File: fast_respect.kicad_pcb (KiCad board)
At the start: 2 copper layers, 70 x 110 mm, 97 parts, among them J1_1 Conn_02x04_Odd_Even, J5_1 Conn_02x03_Odd_Even, J5_2 Conn_02x03_Odd_Even, J7_1 Conn_01x02, Q2_1 AONM7421, Q3_1 IRLML6344T, Q4_1 IRLML6344T, Q4_2 IRLML6344T, Q4_3 IRLML6344T, Q4_4 IRLML6344T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

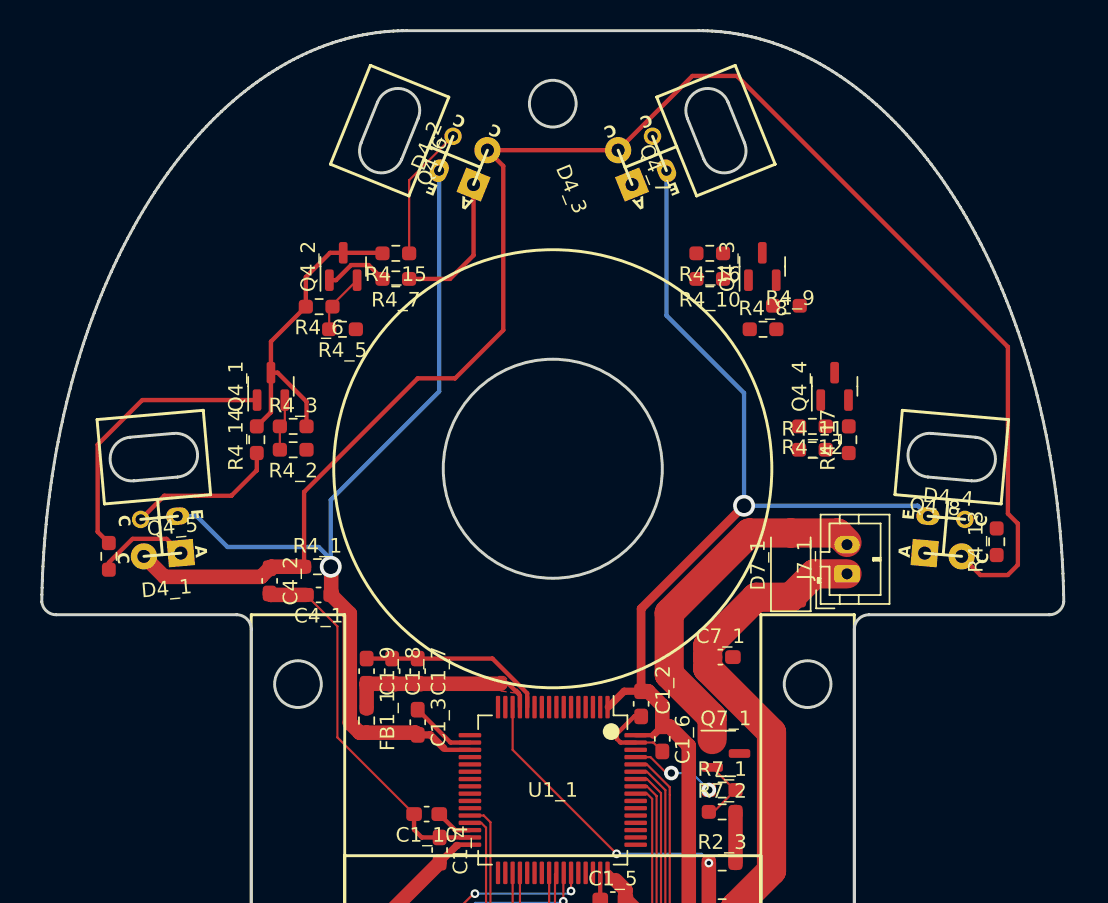
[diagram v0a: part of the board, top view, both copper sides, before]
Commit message: 距離センサ周り引いた
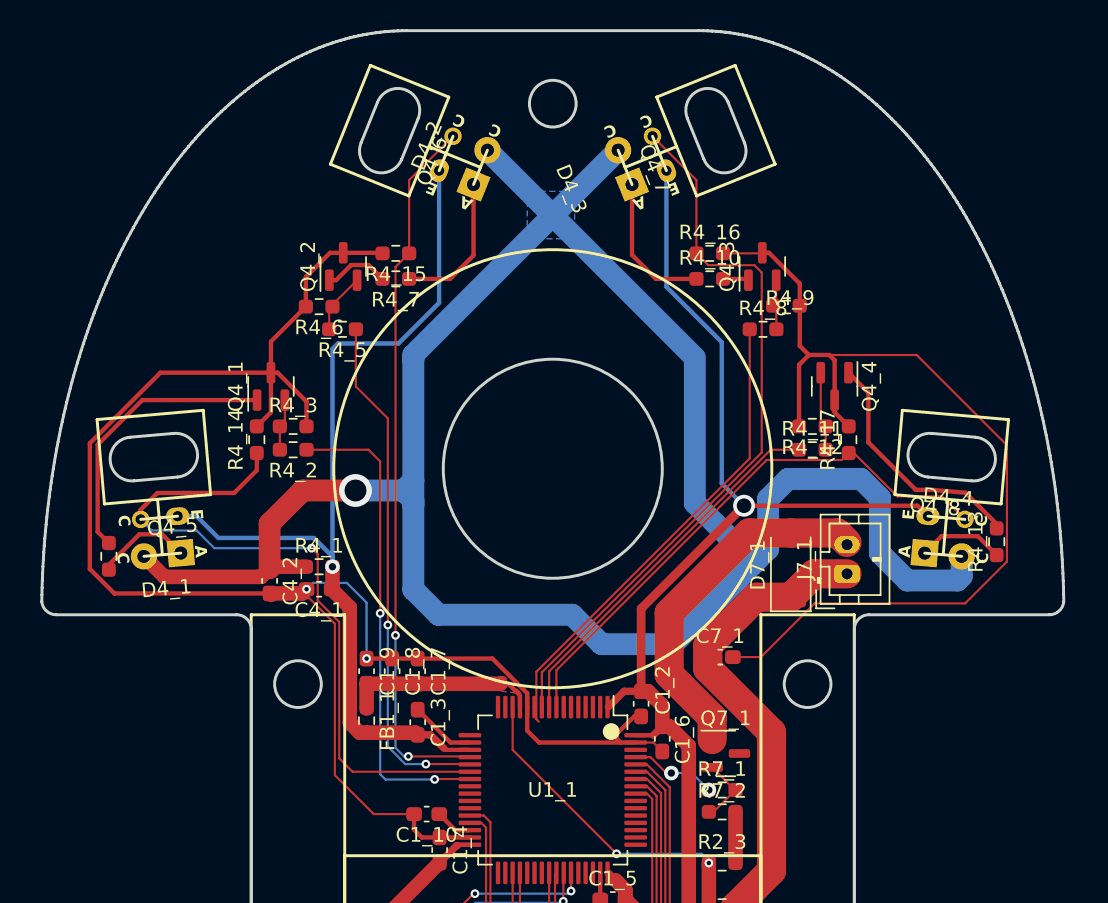
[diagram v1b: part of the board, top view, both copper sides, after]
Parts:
- moved C4_1 0.39 mm to (-51.0, 38.2)
- moved R4_1 0.12 mm to (-51.0, 36.7)
- turned Q4_4 to -90 degrees
- turned R4_10 to 0 degrees
- turned R4_16 to 0 degrees
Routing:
- net GND: track 222.0 -> 346.2 mm, vias 2 -> 4
- net DIST_ADC_3: track 0.00 -> 50.3 mm
- net Net-(D4_1-A): track 113.3 -> 156.0 mm, vias 0 -> 1
- net DIST_ADC_2: track 9.26 -> 48.9 mm, vias 0 -> 2
- net DIST_ADC_4: track 0.00 -> 38.5 mm
- net DIST_ADC_1: track 10.8 -> 48.2 mm, vias 0 -> 1
- net DIST_LED_2: track 0.00 -> 35.6 mm, vias 0 -> 2
- net DIST_LED_1: track 0.14 -> 33.2 mm, vias 0 -> 2
- net DIST_LED_3: track 0.00 -> 33.0 mm
- net DIST_LED_4: track 0.00 -> 25.9 mm
- net Net-(Q4_4-D): track 0.00 -> 16.7 mm
- net Net-(D4_3-K): track 0.00 -> 9.91 mm
- net Net-(D4_4-K): track 0.00 -> 5.95 mm
- net Net-(Q4_4-G): track 0.00 -> 5.42 mm
- net Net-(Q4_3-G): track 0.00 -> 3.86 mm
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- added copper zone on B.Cu, net Net-(D4_1-A)

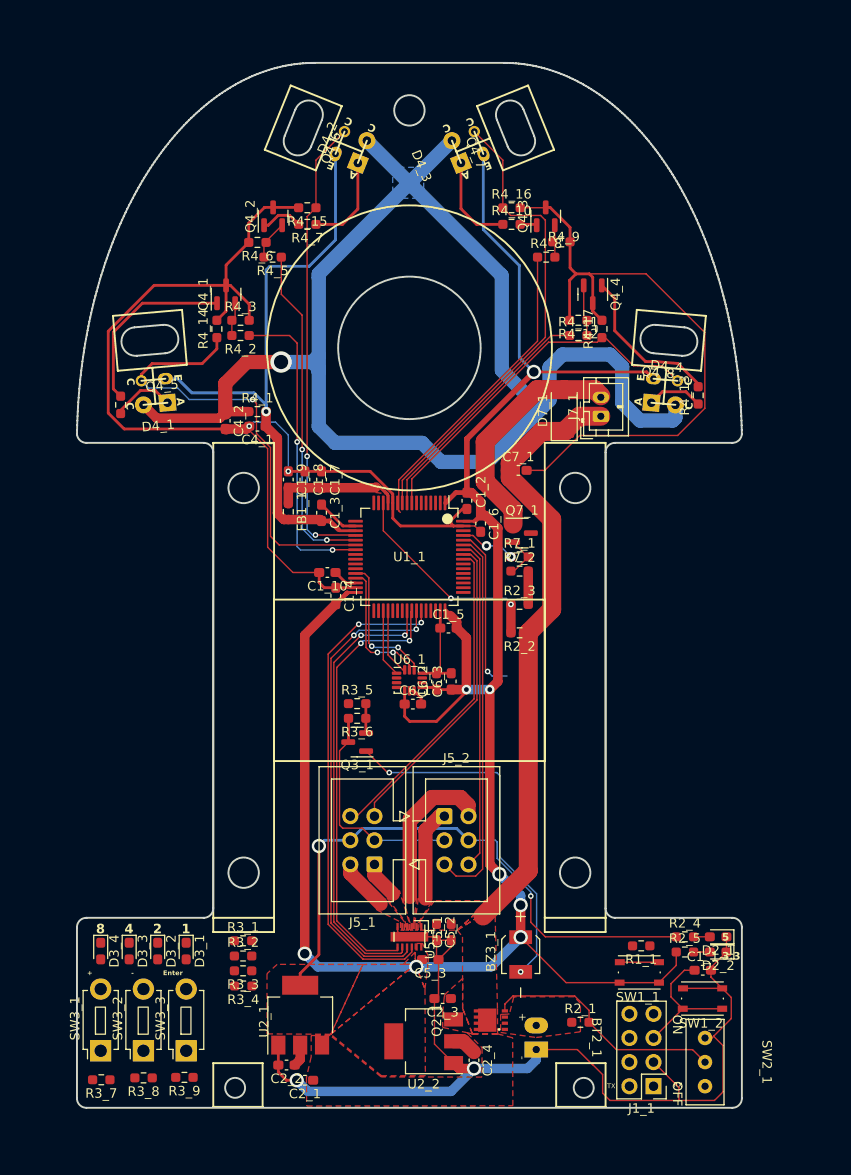
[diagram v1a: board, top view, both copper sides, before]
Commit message: 左側の3.3vのラインを車体前方まで引いた
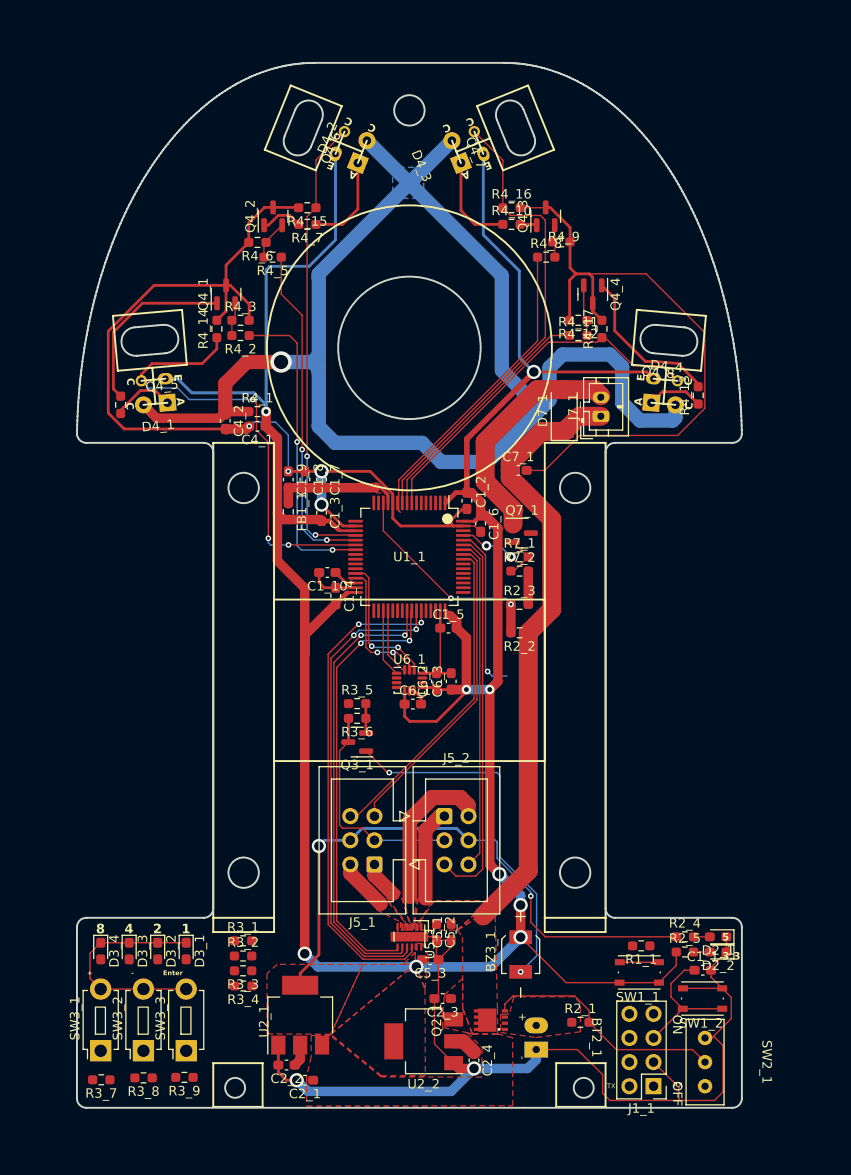
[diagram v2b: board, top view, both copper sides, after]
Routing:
- net +3.3V: track 289.9 -> 305.9 mm
- net GND: track 346.2 -> 353.9 mm, vias 4 -> 6
- net DIST_ADC_1: track 48.2 -> 48.7 mm, vias 1 -> 3

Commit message: 電源周りを整えてUIと書き込み配線以外完成
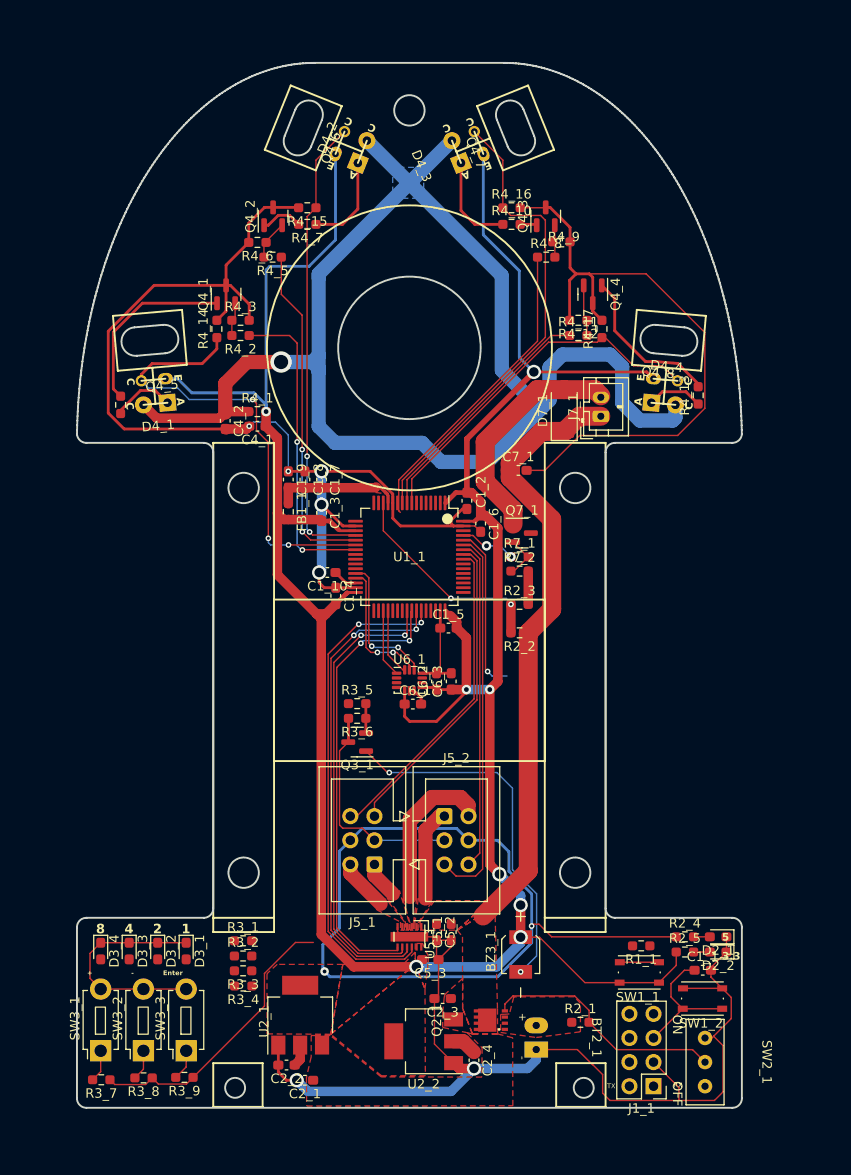
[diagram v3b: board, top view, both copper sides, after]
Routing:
- net +3.3V: track 305.9 -> 330.9 mm, vias 9 -> 8
- net +5V: track 63.8 -> 85.6 mm
- net GND: track 353.9 -> 361.1 mm, vias 6 -> 7
- net UI_SW_1: track 0.00 -> 3.40 mm
- net UI_SW_3: track 0.00 -> 3.26 mm
- net UI_SW_2: track 0.00 -> 3.22 mm

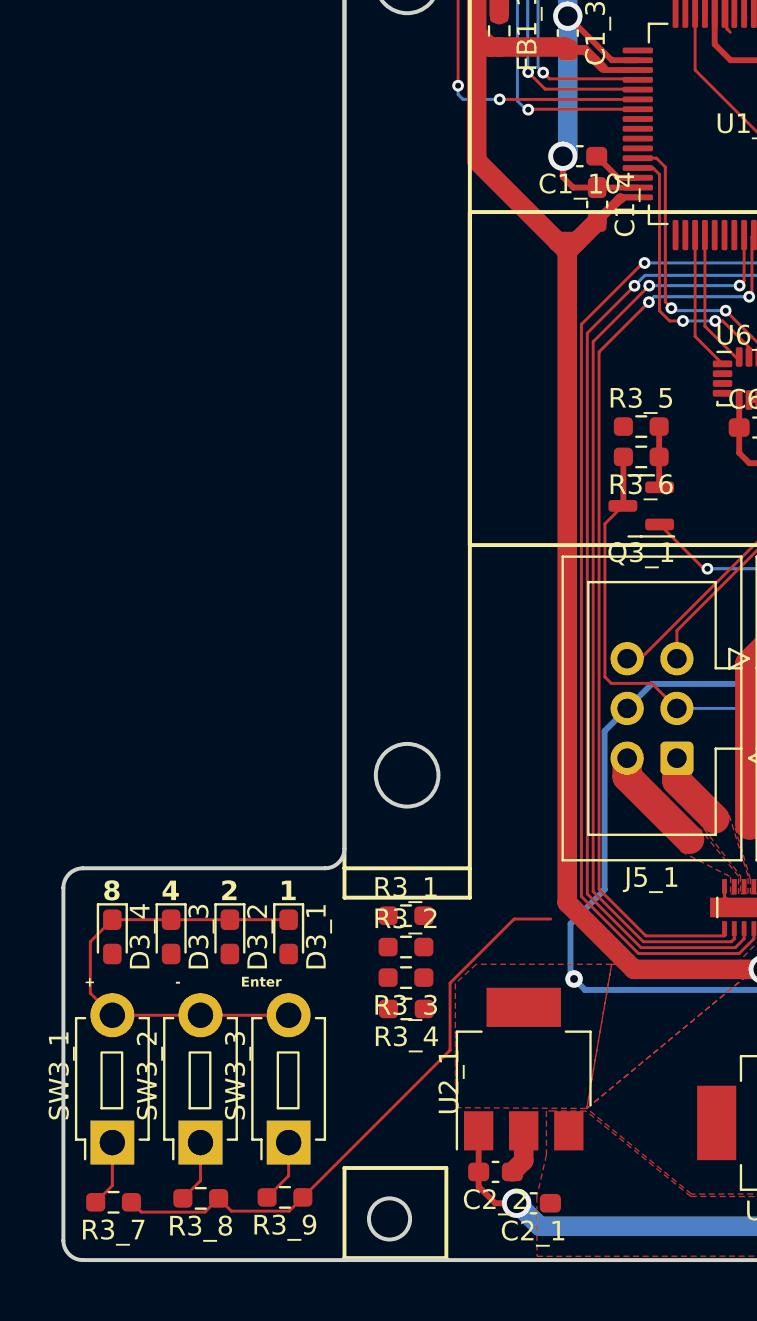
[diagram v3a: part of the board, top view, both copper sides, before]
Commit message: UI_LED接続
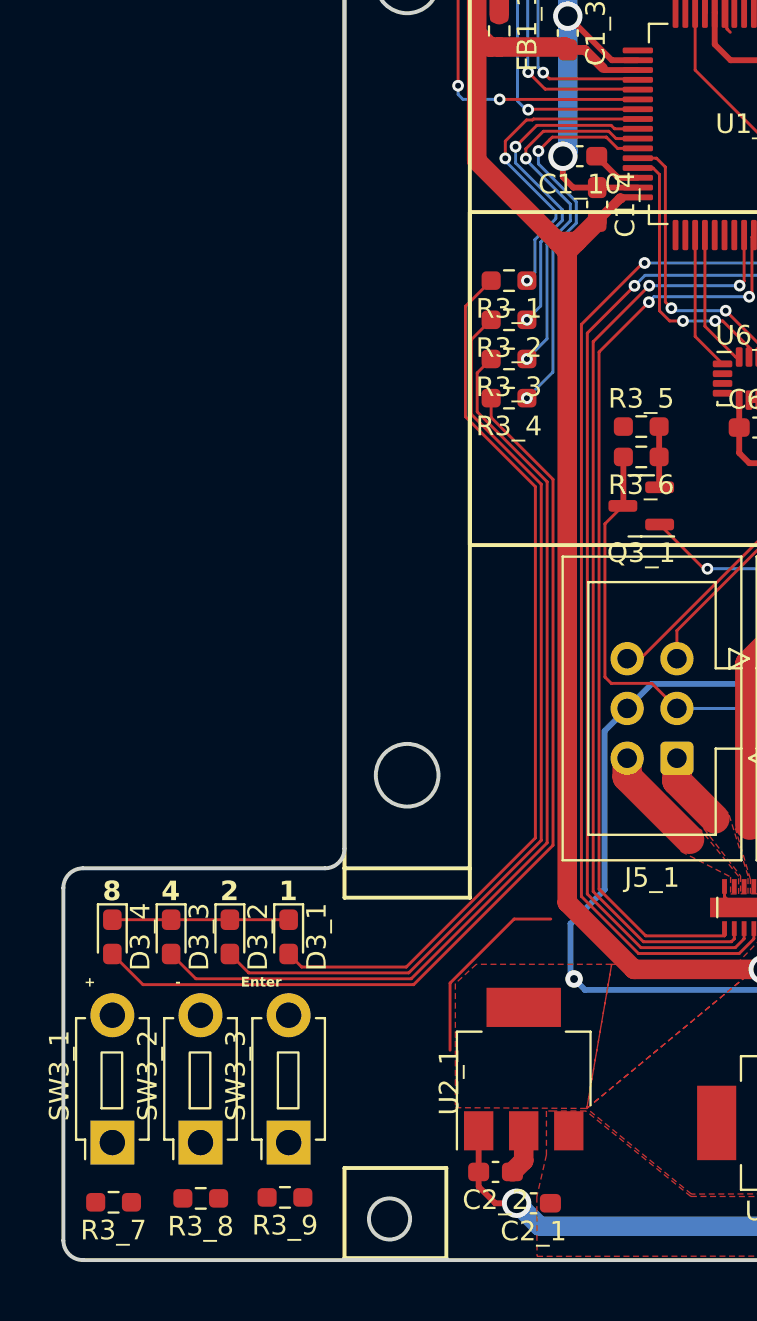
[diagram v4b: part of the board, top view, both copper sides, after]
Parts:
- moved R3_1 32.8 mm to (-47.2, 60.0), turned to 180 degrees
- moved R3_2 32.4 mm to (-47.2, 62.0), turned to 180 degrees
- moved R3_3 32.0 mm to (-47.2, 64.0)
- moved R3_4 31.6 mm to (-47.2, 66.0)
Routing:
- net Net-(D3_4-A): track 0.00 -> 50.2 mm
- net Net-(D3_3-A): track 0.00 -> 49.1 mm
- net Net-(D3_2-A): track 0.00 -> 47.6 mm
- net Net-(D3_1-A): track 0.00 -> 46.1 mm
- net +3.3V: track 330.9 -> 310.5 mm
- net UI_LED_4: track 0.00 -> 20.1 mm, vias 0 -> 2
- net UI_LED_3: track 0.00 -> 18.8 mm, vias 0 -> 2
- net UI_LED_2: track 0.00 -> 17.3 mm, vias 0 -> 2
- net UI_LED_1: track 0.00 -> 16.0 mm, vias 0 -> 2
- net GND: track 361.1 -> 346.3 mm
- net UI_SW_1: track 3.40 -> 0.00 mm
- net UI_SW_3: track 3.26 -> 0.00 mm
- net UI_SW_2: track 3.22 -> 0.00 mm

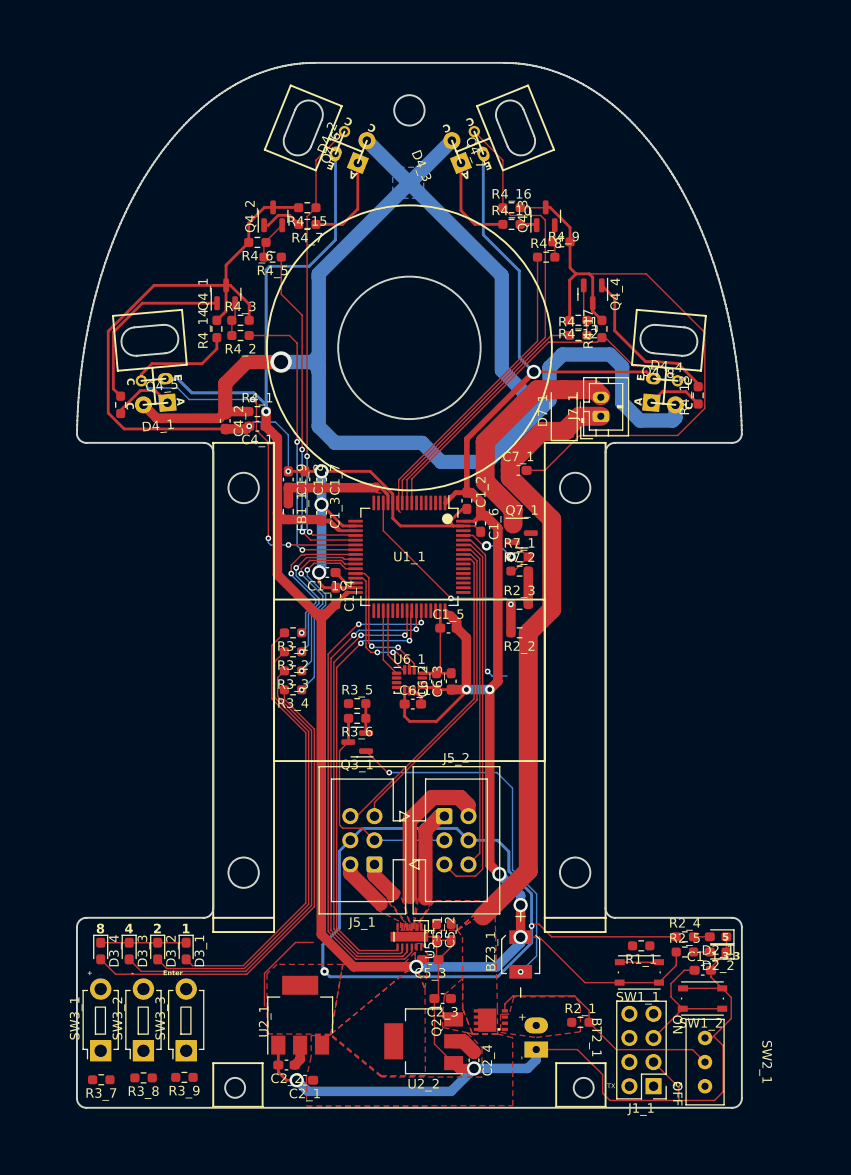
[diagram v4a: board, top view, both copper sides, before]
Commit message: 書き込みピン配線
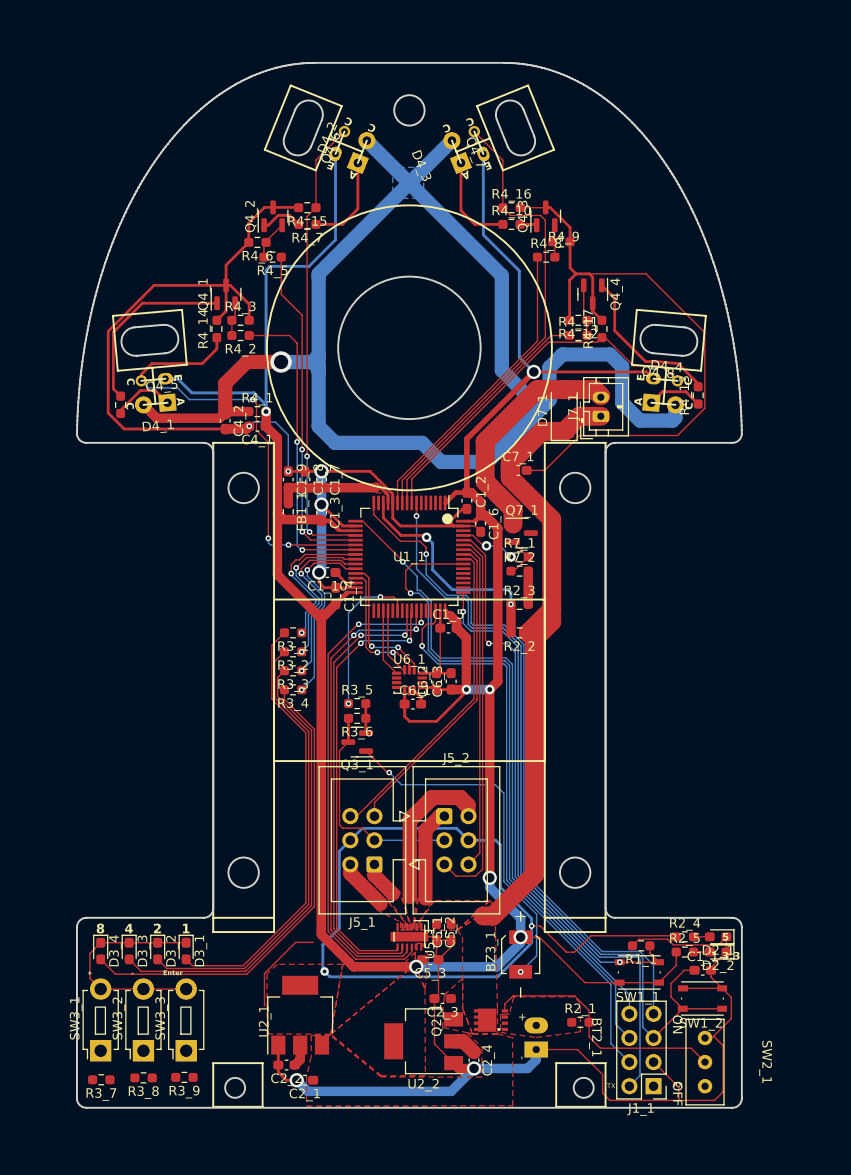
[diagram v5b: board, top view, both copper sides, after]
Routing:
- net TX: track 0.00 -> 72.6 mm, vias 0 -> 1
- net NRST: track 14.7 -> 86.8 mm, vias 0 -> 1
- net SWO: track 0.00 -> 69.9 mm, vias 0 -> 1
- net RX: track 0.00 -> 68.5 mm, vias 0 -> 1
- net SWCLK: track 0.00 -> 64.4 mm, vias 0 -> 1
- net SWDIO: track 0.00 -> 61.6 mm, vias 0 -> 1
- net BOOT0: track 21.7 -> 60.2 mm, vias 1 -> 2
- net GND: track 346.3 -> 371.9 mm
- net BUZZER_PWM: track 0.00 -> 16.6 mm, vias 0 -> 2
- net +8V: track 64.5 -> 69.5 mm
- net BAT_ADC: track 22.7 -> 24.1 mm
- net +5V: track 85.6 -> 86.8 mm
- net DIST_LED_3: track 33.0 -> 32.0 mm
- net Net-(Q2_1-G): track 25.8 -> 26.7 mm
- net Net-(Q3_1-D): track 38.1 -> 37.3 mm
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
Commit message: UIスイッチ配線完了
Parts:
- moved Q3_1 1.00 mm to (-39.5, 71.5)
- moved R3_5 1.00 mm to (-39.5, 67.5)
- moved R3_6 1.00 mm to (-39.5, 69.0)
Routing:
- net UI_SW_1: track 0.00 -> 81.1 mm, vias 0 -> 1
- net UI_SW_2: track 0.00 -> 76.4 mm, vias 0 -> 1
- net UI_SW_3: track 0.00 -> 71.7 mm, vias 0 -> 1
- net BUZZER_PWM: track 16.6 -> 17.7 mm
- net SWO: track 69.9 -> 69.0 mm
- net Net-(Q3_1-D): track 37.3 -> 36.7 mm
